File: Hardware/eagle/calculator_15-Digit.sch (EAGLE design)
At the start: 145 parts, among them IC1 74HC4053P, M1 IRLML6402, M10 IRLML6402, M11 IRLML6402, M12 IRLML6402, M2 IRLML6402, M3 IRLML6402, M4 IRLML6402, M5 IRLML6402, M6 IRLML6402, M7 IRLML6402, M8 IRLML6402, M9 IRLML6402, U1 74HC4051_MUXDIL_16, U2 TC1262-3.3VDB, U3 ATMEGA1284P-PU, U5 CON, X1 MICROMATCH-12, X2 MICROMATCH-12, X3 MICROMATCH-12, X4 MICROMATCH-12, Y2 12MHz

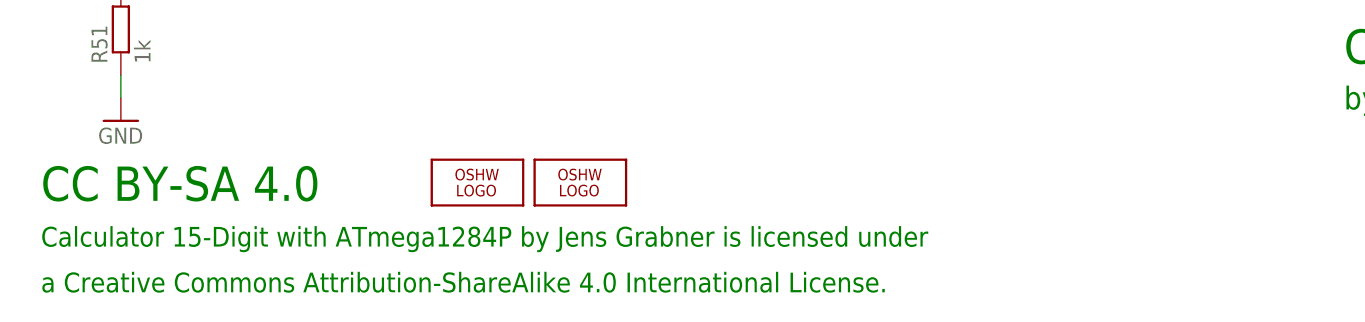
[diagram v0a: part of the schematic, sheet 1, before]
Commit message: change switch from x^3 to INT and invers
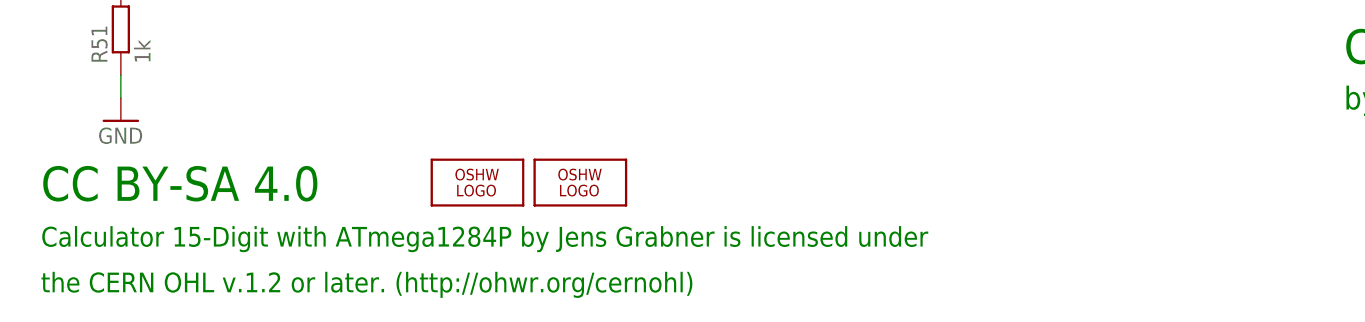
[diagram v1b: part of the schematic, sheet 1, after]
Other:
- note added: "the CERN OHL v.1.2 or later. (http://ohwr.org/cernohl)"
- note removed: "a Creative Commons Attribution-ShareAlike 4.0 International License."
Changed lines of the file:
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@@
 <text x="5.08" y="10.16" size="2.1844" layer="91" ratio="10">Calculator 15-Digit with ATmega1284P by Jens Grabner is licensed under</text>
 <text x="5.08" y="15.24" size="3.81" layer="91" ratio="12">CC BY-SA 4.0</text>
-<text x="5.08" y="5.08" size="2.1844" layer="91" ratio="10">a Creative Commons Attribution-ShareAlike 4.0 International License.</text>
+<text x="5.08" y="5.08" size="2.1844" layer="91" ratio="10">the CERN OHL v.1.2 or later. (http://ohwr.org/cernohl)</text>
 </plain>
 <instances>
@@
 <text x="5.08" y="10.16" size="2.1844" layer="91" ratio="10">Calculator 15-Digit with ATmega1284P by Jens Grabner is licensed under</text>
 <text x="5.08" y="15.24" size="3.81" layer="91" ratio="12">CC BY-SA 4.0</text>
-<text x="5.08" y="5.08" size="2.1844" layer="91" ratio="10">a Creative Commons Attribution-ShareAlike 4.0 International License.</text>
+<text x="5.08" y="5.08" size="2.1844" layer="91" ratio="10">the CERN OHL v.1.2 or later. (http://ohwr.org/cernohl)</text>
 </plain>
 <instances>
@@
 <text x="-203.2" y="38.1" size="2.1844" layer="91" ratio="10">Calculator 15-Digit with ATmega1284P by Jens Grabner is licensed under</text>
 <text x="-203.2" y="43.18" size="3.81" layer="91" ratio="12">CC BY-SA 4.0</text>
-<text x="-203.2" y="33.02" size="2.1844" layer="91" ratio="10">a Creative Commons Attribution-ShareAlike 4.0 International License.</text>
+<text x="-203.2" y="33.02" size="2.1844" layer="91" ratio="10">the CERN OHL v.1.2 or later. (http://ohwr.org/cernohl)</text>
 </plain>
 <instances>

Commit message: Switch-block changed Rev.02
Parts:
- removed BAT1, BAT2, BAT3: NimH_AAA, SparkFun-Electromechanical:BATTERYAAA-KIT
- added BH1, BH2, BH3: BATTERY_HOLDER_AAAHOLDER_AAA, SparkFun-Electromechanical:BATTERY_HOLDER_AAAHOLDER_AAA
- added U$4, U$5: HOLDER_AAA_LEFT1, SparkFun-Electromechanical:HOLDER_AAA_LEFT1
- added U$6: HOLDER_AAA_RIGHT, SparkFun-Electromechanical:HOLDER_AAA_RIGHT
- D14, D15, D16, D17, D18, D19, D2, D20, D21, D22, D23, D24, D25, D26, D27: value SC40-11_UNI -> SC40-11_UNISC40-11_UNI; device display-hp:SC40-11_UNI -> display-hp:SC40-11_UNISC40-11_UNI
- R10, R11, R12, R13, R14, R15, R16, R17, R18, R19, R5, R6, R7, R8, R9: device rcl:R-EU_0204/7 -> rcl:R-EU_R1210
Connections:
- new net NC1: U$4.+
- new net NC2: U$5.+
- new net NC3: U$6.-
- net DIG_0: now also D2.CC2, D2.CC3, D2.CC4; no longer D2.CC, D2.CC@1, D2.CC@2
- net DIG_1: now also D14.CC2, D14.CC3, D14.CC4; no longer D14.CC, D14.CC@1, D14.CC@2
- net DIG_10: now also D23.CC2, D23.CC3, D23.CC4; no longer D23.CC, D23.CC@1, D23.CC@2
- net DIG_11: now also D24.CC2, D24.CC3, D24.CC4; no longer D24.CC, D24.CC@1, D24.CC@2
- net DIG_12: now also D25.CC2, D25.CC3, D25.CC4; no longer D25.CC, D25.CC@1, D25.CC@2
- net DIG_13: now also D26.CC2, D26.CC3, D26.CC4; no longer D26.CC, D26.CC@1, D26.CC@2
- net DIG_14: now also D27.CC2, D27.CC3, D27.CC4; no longer D27.CC, D27.CC@1, D27.CC@2
- net DIG_2: now also D15.CC2, D15.CC3, D15.CC4; no longer D15.CC, D15.CC@1, D15.CC@2
- net DIG_3: now also D16.CC2, D16.CC3, D16.CC4; no longer D16.CC, D16.CC@1, D16.CC@2
- net DIG_4: now also D17.CC2, D17.CC3, D17.CC4; no longer D17.CC, D17.CC@1, D17.CC@2
- net DIG_5: now also D18.CC2, D18.CC3, D18.CC4; no longer D18.CC, D18.CC@1, D18.CC@2
- net DIG_6: now also D19.CC2, D19.CC3, D19.CC4; no longer D19.CC, D19.CC@1, D19.CC@2
- net DIG_7: now also D20.CC2, D20.CC3, D20.CC4; no longer D20.CC, D20.CC@1, D20.CC@2
- net DIG_8: now also D21.CC2, D21.CC3, D21.CC4; no longer D21.CC, D21.CC@1, D21.CC@2
- net DIG_9: now also D22.CC1, D22.CC2, D22.CC3, D22.CC4; no longer D22.CC, D22.CC@1
- net GND: now also BH1.-; no longer BAT3.-
- net N$2: now also BH1.+, BH2.-; no longer BAT2.-, BAT3.+
- net N$3: now also BH2.+, BH3.-; no longer BAT1.-, BAT2.+
- net SEG_C: now also D14.C, D15.C, D16.C, D17.C, D18.C, D19.C, D2.C, D20.C, D21.C, D22.C, D23.C, D24.C, D25.C, D26.C, D27.C; no longer D14.C1, D15.C1, D16.C1, D17.C1, D18.C1, D19.C1, D2.C1, D20.C1, D21.C1, D22.C1, D23.C1, D24.C1, D25.C1, D26.C1, D27.C1
- net VCC: now also BH3.+; no longer BAT1.+
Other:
- note added: "Copyright CERN 2013"
- note removed: "CC BY-SA 4.0"
- moved on the sheet: D14, D15, D16, D17, D18, D19, D2, D20, D21, D22, D23, D24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

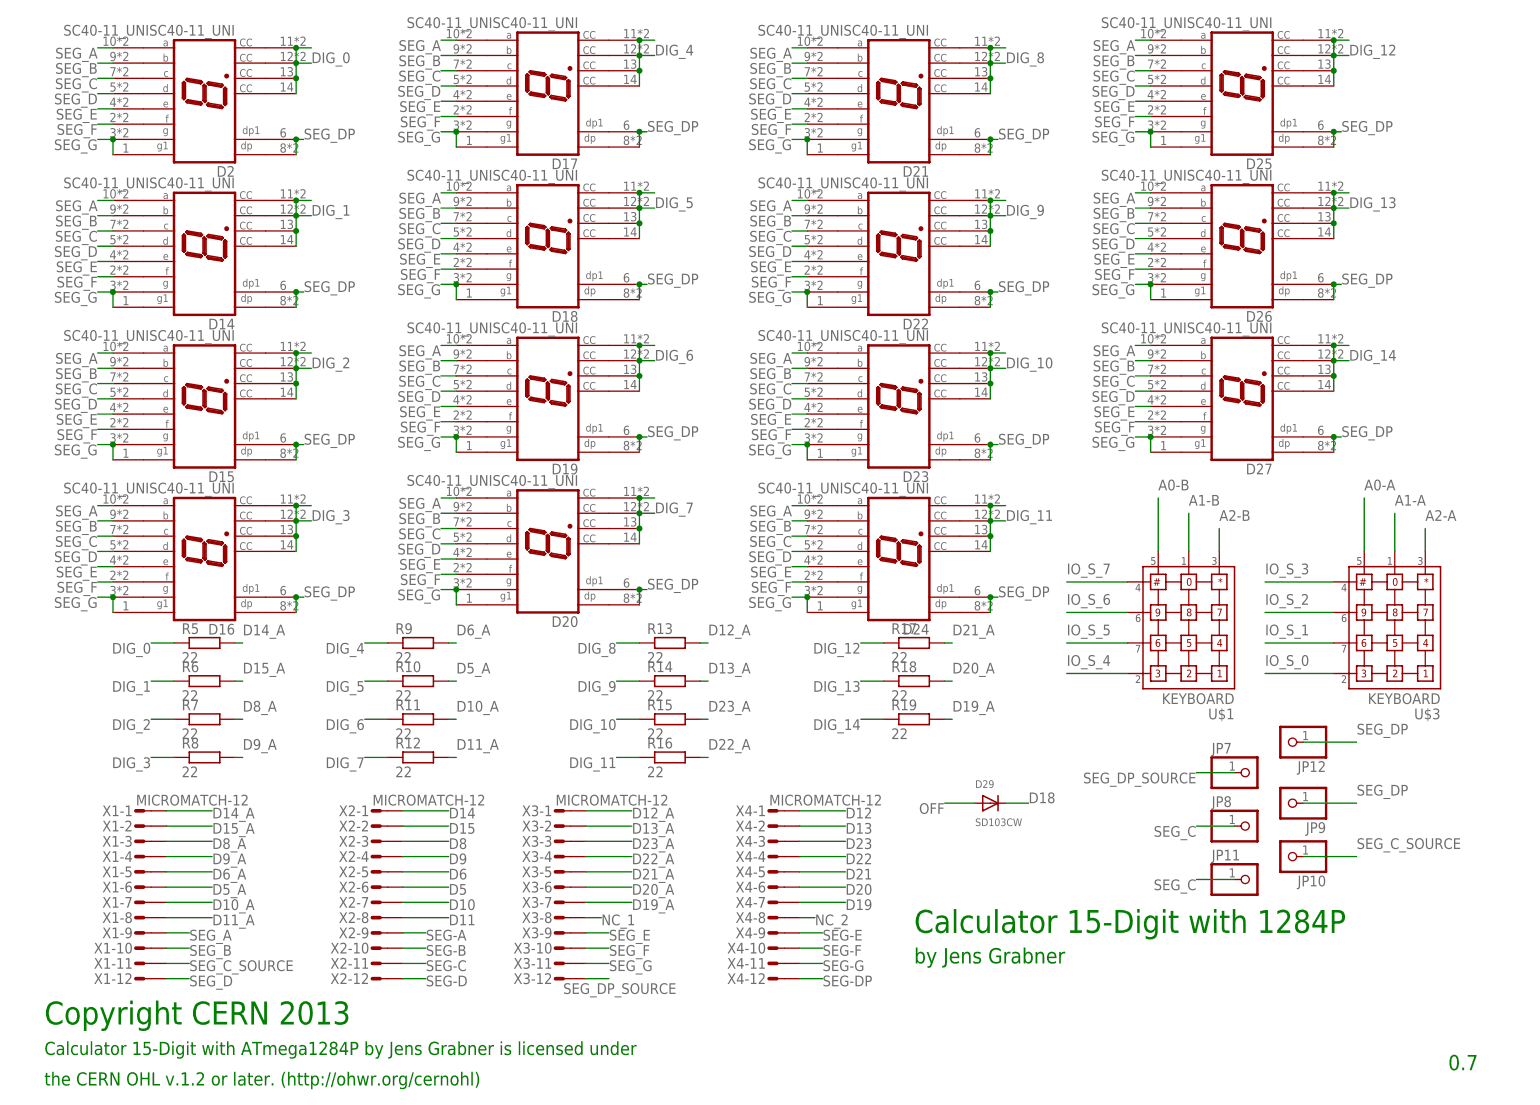
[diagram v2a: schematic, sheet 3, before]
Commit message: Switch-block Filter added
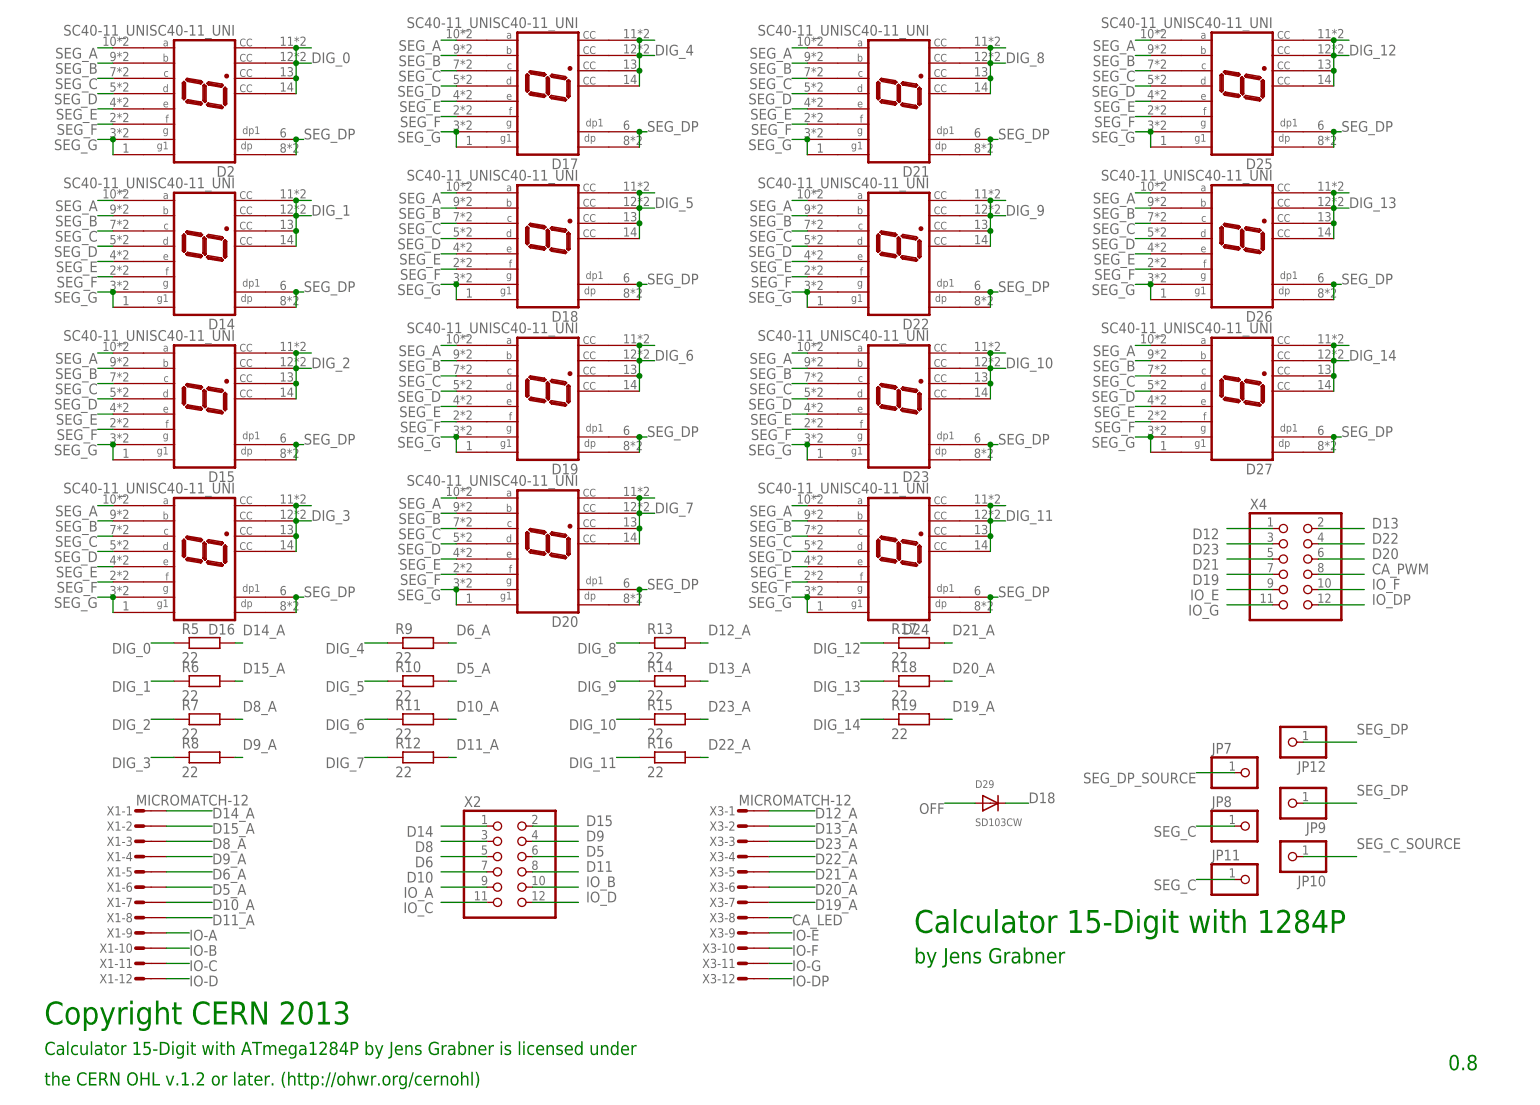
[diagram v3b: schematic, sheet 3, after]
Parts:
- removed D10, D11, D12, D13, D6, D7, D8, D9: SD103CW, BaseApp:DIODESMA
- removed IC1: 74HC4053P, 74xx-eu:74HC4053P
- removed U$1, U$3: KEYBOARD, &my:KEYBOARD
- R36, R37, R38, R39, R40, R41, R42, R43: device rcl:R-EU_0204/7 -> rcl:R-EU_R0805
- U1: value 74HC4051_MUXDIL_16 -> 74HC4051_MUX; device SparkFun-AnalogIC:74HC4051_MUXDIL_16 -> SparkFun-AnalogIC:74HC4051_MUX
- X2, X4: value MICROMATCH-12 -> (none); device Con-amp-micromatch:MICROMATCH-12 -> pinhead:PINHD-2X6
- renumbered U$4 to BH4, U$5 to BH5, U$6 to BH6
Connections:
- removed net A0-A: IC1G$1.1Y0, KP2.C2, U$3.5
- removed net A0-B: IC1G$1.1Y1, KP1.C2, U$1.5
- removed net A1-A: IC1G$1.2Y0, KP2.C1, U$3.1
- removed net A1-B: IC1G$1.2Y1, KP1.C1, U$1.1
- removed net A2-A: IC1G$1.3Y0, KP2.C0, U$3.3
- removed net A2-B: IC1G$1.3Y1, KP1.C0, U$1.3
- removed net IO_0: D10.C, M4.G, R36.2, U1.IO0
- removed net IO_1: D11.C, M5.G, R37.2, U1.IO1
- removed net IO_2: D12.C, M6.G, R42.2, U1.IO3
- removed net IO_3: D13.C, M7.G, R38.2, U1.IO2
- removed net IO_4: D6.C, M8.G, R43.2, U1.IO6
- removed net IO_5: D7.C, M9.G, R39.2, U1.IO7
- removed net IO_6: D8.C, M10.G, R40.2, U1.IO5
- removed net IO_7: D9.C, M11.G, R41.2, U1.IO4
- removed net IO_S_0: D10.A, KP2.R0, U$3.2
- removed net IO_S_1: D11.A, KP2.R1, U$3.7
- removed net IO_S_2: D12.A, KP2.R2, U$3.6
- removed net IO_S_3: D13.A, KP2.R3, U$3.4
- removed net IO_S_4: D6.A, KP1.R0, U$1.2
- removed net IO_S_5: D7.A, KP1.R1, U$1.7
- removed net IO_S_6: D8.A, KP1.R2, U$1.6
- removed net IO_S_7: D9.A, KP1.R3, U$1.4
- removed net N$33: M10.S, M11.S, M3.D, M4.S, M5.S, M6.S, M7.S, M8.S, M9.S, R33.1, R36.1, R37.1, R38.1, R39.1, R40.1, R41.1, R42.1, R43.1
- removed net NC_1: X3-8.S
- removed net NC_2: X4-8.S
- removed net SEG-A: M4.D, X2-9.S
- removed net SEG-B: M5.D, X2-10.S
- removed net SEG-C: M6.D, X2-11.S
- removed net SEG-D: M7.D, X2-12.S
- removed net SEG-DP: M11.D, X4-12.S
- removed net SEG-E: M8.D, X4-9.S
- removed net SEG-F: M9.D, X4-10.S
- removed net SEG-G: M10.D, X4-11.S
- new net CA_LED: M10.S, M11.S, M4.S, M5.S, M6.S, M7.S, M8.S, M9.S, R36.1, R37.1, R38.1, R39.1, R40.1, R41.1, R42.1, R43.1, X3-8.S
- new net CA_PWM: M3.D, R33.1, X4.8
- new net IO-A: M4.G, R36.2, X1-9.S
- new net IO-B: M5.G, R37.2, X1-10.S
- new net IO-C: M6.G, R42.2, X1-11.S
- new net IO-D: M7.G, R38.2, X1-12.S
- new net IO-DP: M11.G, R41.2, X3-12.S
- new net IO-E: M8.G, R43.2, X3-9.S
- new net IO-F: M9.G, R39.2, X3-10.S
- new net IO-G: M10.G, R40.2, X3-11.S
- new net IO_A: KP2.R0, U1.IO0, X2.9
- new net IO_B: KP2.R1, U1.IO1, X2.10
- new net IO_C: KP2.R2, U1.IO3, X2.11
- new net IO_D: KP2.R3, U1.IO2, X2.12
- new net IO_DP: KP1.R3, U1.IO4, X4.12
- new net IO_E: KP1.R0, U1.IO6, X4.9
- new net IO_F: KP1.R1, U1.IO7, X4.10
- new net IO_G: KP1.R2, U1.IO5, X4.11
- net A1: no longer IC1G$1.S1, IC1G$1.S2, IC1G$1.S3
- net A_0: now also KP1.C2, KP2.C2; no longer IC1G$1.1Z
- net A_1: now also KP1.C1, KP2.C1; no longer IC1G$1.2Z
- net A_2: now also KP1.C0, KP2.C0; no longer IC1G$1.3Z
- net D10: now also X2.7; no longer X2-7.S
- net D11: now also X2.8; no longer X2-8.S
- net D12: now also X4.1; no longer X4-1.S
- net D13: now also X4.2; no longer X4-2.S
- net D14: now also X2.1; no longer X2-1.S
- net D15: now also X2.2; no longer X2-2.S
- net D19: now also X4.7; no longer X4-7.S
- net D20: now also X4.6; no longer X4-6.S
- net D21: now also X4.5; no longer X4-5.S
- net D22: now also X4.4; no longer X4-4.S
- net D23: now also X4.3; no longer X4-3.S
- net D5: now also X2.6; no longer X2-6.S
- net D6: now also X2.5; no longer X2-5.S
- net D8: now also X2.3; no longer X2-3.S
- net D9: now also X2.4; no longer X2-4.S
- net GND: no longer IC1P.GND, IC1P.VEE
- net INH: no longer IC1G$1.E
- net SEG_A: now also M4.D; no longer X1-9.S
- net SEG_B: now also M5.D; no longer X1-10.S
- net SEG_C_SOURCE: now also M6.D; no longer X1-11.S
- net SEG_D: now also M7.D; no longer X1-12.S
- net SEG_DP_SOURCE: now also M11.D; no longer X3-12.S
- net SEG_E: now also M8.D; no longer X3-9.S
- net SEG_F: now also M9.D; no longer X3-10.S
- net SEG_G: now also M10.D; no longer X3-11.S
- net V_IN: no longer IC1P.VCC
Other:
- note added: "0.8"
- note removed: "0.7"
- moved on the sheet: X3-1, X3-10, X3-11, X3-12, X3-2, X3-3, X3-4, X3-5, X3-6, X3-7, X3-8, X3-9

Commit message: Debuglevel 13 - Protokoll Statepoint
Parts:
- added R29, R30, R54, R55, R56, R57, R58, R59: 3k3, rcl:R-EU_0204/5
- R36, R37, R38, R39, R40, R41, R42, R43: device rcl:R-EU_R0805 -> rcl:R-EU_R1206
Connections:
- removed net D15_A: R6.2, X1-2.S
- removed net D19_A: R19.2, X3-7.S
- removed net D20_A: R18.2, X3-6.S
- removed net D21_A: R17.2, X3-5.S
- removed net D22_A: R16.2, X3-4.S
- removed net D23_A: R15.2, X3-3.S
- new net D0_A: R5.2, X3-1.S
- new net D1_A: R6.2, X3-2.S
- new net D2_A: R7.2, X3-3.S
- new net D3_A: R8.2, X3-4.S
- new net D4_A: R9.2, X3-5.S
- new net D7_A: R12.2, X1-5.S
- new net IO_A__: X2.9
- new net IO_B__: X2.10
- new net IO_C__: X2.11
- new net IO_D__: X2.12
- net CA_LED: now also R29.1, R30.1, R54.1, R55.1, R56.1, R57.1, R58.1, R59.1
- net D10_A: now also R15.2, X1-8.S; no longer R11.2, X1-7.S
- net D11_A: now also R16.2, X1-9.S; no longer R12.2, X1-8.S
- net D12_A: now also R17.2, X1-10.S; no longer R13.2, X3-1.S
- net D13_A: now also R18.2, X1-11.S; no longer R14.2, X3-2.S
- net D14: no longer X2.1
- net D14_A: now also R19.2, X1-12.S; no longer R5.2, X1-1.S
- net D15: no longer X2.2
- net D5_A: now also X3-6.S; no longer X1-6.S
- net D6_A: now also R11.2, X3-7.S; no longer R9.2, X1-5.S
- net D8: no longer X2.3
- net D8_A: now also R13.2, X1-6.S; no longer R7.2, X1-3.S
- net D9: no longer X2.4
- net D9_A: now also R14.2, X1-7.S; no longer R8.2, X1-4.S
- net IO-A: now also R29.2, X1-4.S; no longer X1-9.S
- net IO-B: now also R30.2, X1-3.S; no longer X1-10.S
- net IO-C: now also R54.2, X1-2.S; no longer X1-11.S
- net IO-D: now also R55.2, X1-1.S; no longer X1-12.S
- net IO-DP: now also R59.2, X3-9.S; no longer X3-12.S
- net IO-E: now also R56.2, X3-12.S; no longer X3-9.S
- net IO-F: now also R57.2, X3-11.S; no longer X3-10.S
- net IO-G: now also R58.2, X3-10.S; no longer X3-11.S
- net IO_A: now also X2.4; no longer X2.9
- net IO_B: now also X2.3; no longer X2.10
- net IO_C: now also X2.2; no longer X2.11
- net IO_D: now also X2.1; no longer X2.12
- net IO_DP: now also X4.9; no longer X4.12
- net IO_E: now also X4.12; no longer X4.9
- net IO_F: now also X4.11; no longer X4.10
- net IO_G: now also X4.10; no longer X4.11
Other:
- moved on the sheet: R36

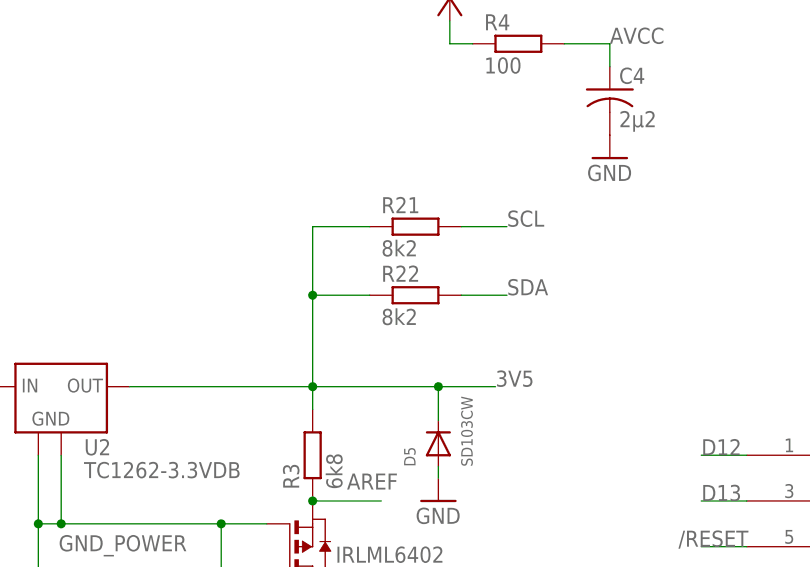
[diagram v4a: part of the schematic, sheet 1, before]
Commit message: snc98_Display_15x7-Segment_LED_v2
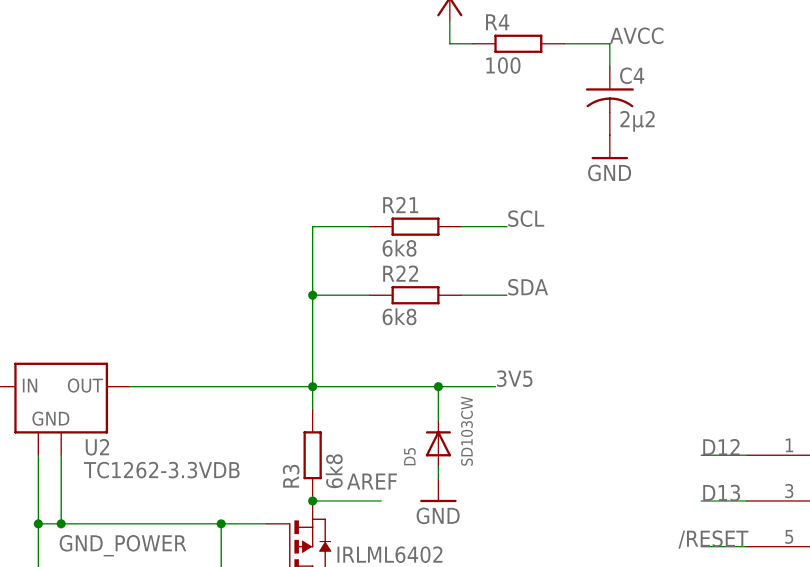
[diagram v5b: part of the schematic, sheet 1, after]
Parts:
- R21, R22: value 8k2 -> 6k8
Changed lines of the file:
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@@
 <part name="R18" library="rcl" deviceset="R-EU_" device="R1210" value="22"/>
 <part name="R19" library="rcl" deviceset="R-EU_" device="R1210" value="22"/>
-<part name="R21" library="rcl" deviceset="R-EU_" device="0204/7" value="8k2"/>
-<part name="R22" library="rcl" deviceset="R-EU_" device="0204/7" value="8k2"/>
+<part name="R21" library="rcl" deviceset="R-EU_" device="0204/7" value="6k8"/>
+<part name="R22" library="rcl" deviceset="R-EU_" device="0204/7" value="6k8"/>
 <part name="R23" library="rcl" deviceset="R-EU_" device="0204/7" value="27k"/>
 <part name="R24" library="rcl" deviceset="R-EU_" device="0204/7" value="6k8"/>
